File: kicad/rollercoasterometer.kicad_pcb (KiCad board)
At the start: 2 copper layers, 61 x 94 mm, 112 parts, among them J120 STANDOFF, J125 STANDOFF, J127 STANDOFF, J129 STANDOFF, J1401 USB_C_Receptacle, J1402 USB_C_Receptacle, J1601 USB_C_Receptacle, J1602 USB_C_Receptacle, J401 SMA, Q2001 NMOS, Q3101 NMOS, Q801 NMOS, U1001 ADP122 1.8V, U104 Teensy4.1, U1101 BMM150, U1201 ICM-42688, U1301 ICM-42688, U1801 TLE493D-W2B6, U1901 ADP122 1.8V, U201 ICM-42688, U2101 ICM-42688, U2201 BMM150, U2401 AK09918, U2501 BMP384, U2701 ICM-42688, U2801 TLE493D-W2B6, U2901 BMP384, U3001 ADP122 1.8V, U301 USBLC6-2SC6, U3201 ICM-42688, U3301 BMM150, U3401 AK09918, U401 ZED_F9R, U501 ADP122 1.8V, U601 AK09918, U704 TLE493D-W2B6, U901 BMP384

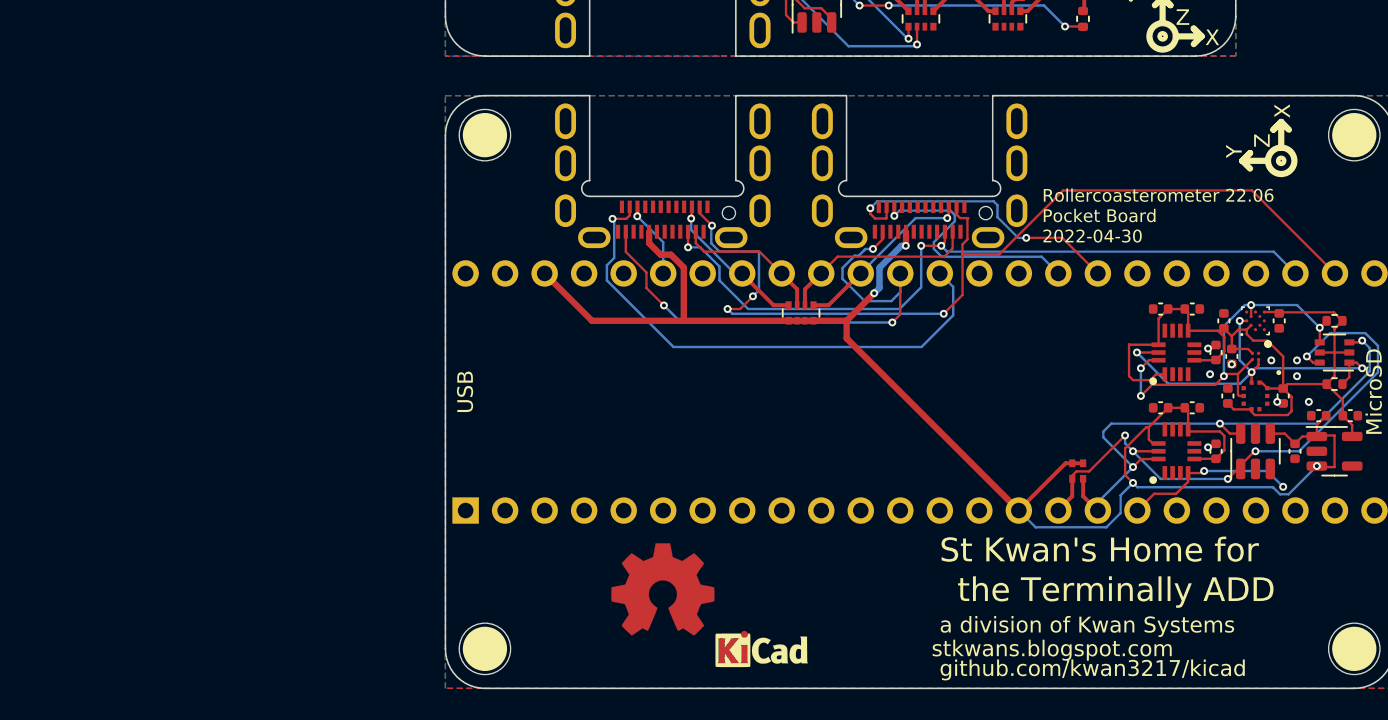
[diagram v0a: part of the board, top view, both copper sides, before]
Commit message: Broke down sensor block into a tree of sheets
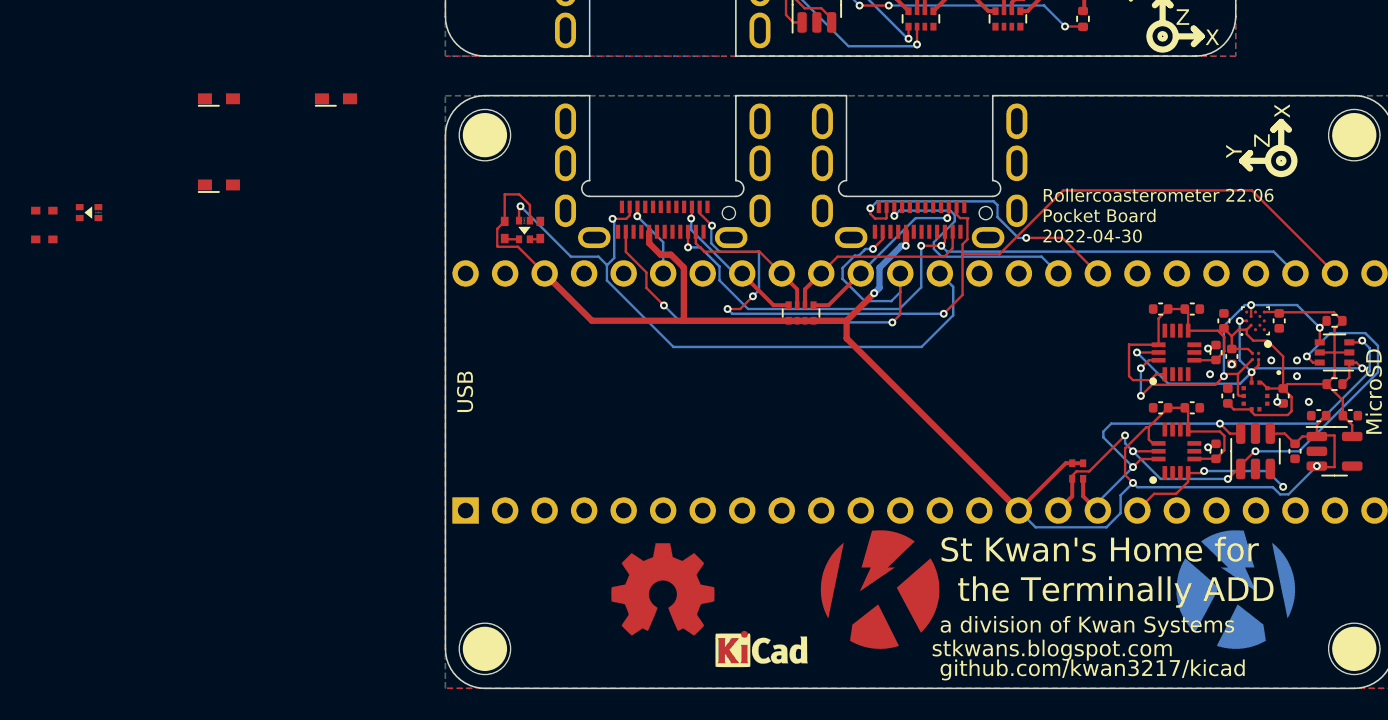
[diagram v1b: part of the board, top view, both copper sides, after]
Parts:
- added D1001: RED, KwanSystems:D_KINGBRIGHT, F.Cu at (69.2, 117.0)
- added D1401: GREEN, YELLOW, KwanSystems:LEDKingbrightAPHB, F.Cu at (81.3, 125.5)
- added D1601: GREEN, YELLOW, KwanSystems:LEDKingbrightAPHB, F.Cu at (53.3, 124.4)
- added D1905: RED, KwanSystems:D_KINGBRIGHT, F.Cu at (61.6, 122.6)
- added D3001: RED, KwanSystems:D_KINGBRIGHT, F.Cu at (61.6, 117.0)
- added R1401: 330, KwanSystems:SMD_0402, F.Cu at (82.3, 125.5)
- added R1402: 1k, KwanSystems:SMD_0402, F.Cu at (80.0, 125.5)
- added R1601: 330, KwanSystems:SMD_0402, F.Cu at (50.4, 124.2)
- added R1602: 1k, KwanSystems:SMD_0402, F.Cu at (50.4, 126.1)
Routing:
- net +3V3: track 105.2 -> 115.4 mm
- net /P0_ID: track 33.9 -> 42.0 mm, vias 1 -> 2
- net /Shoe/USB+ cable/DY-: track 0.00 -> 0.94 mm
- net /Shoe/USB+ cable/DG-: track 0.00 -> 0.69 mm

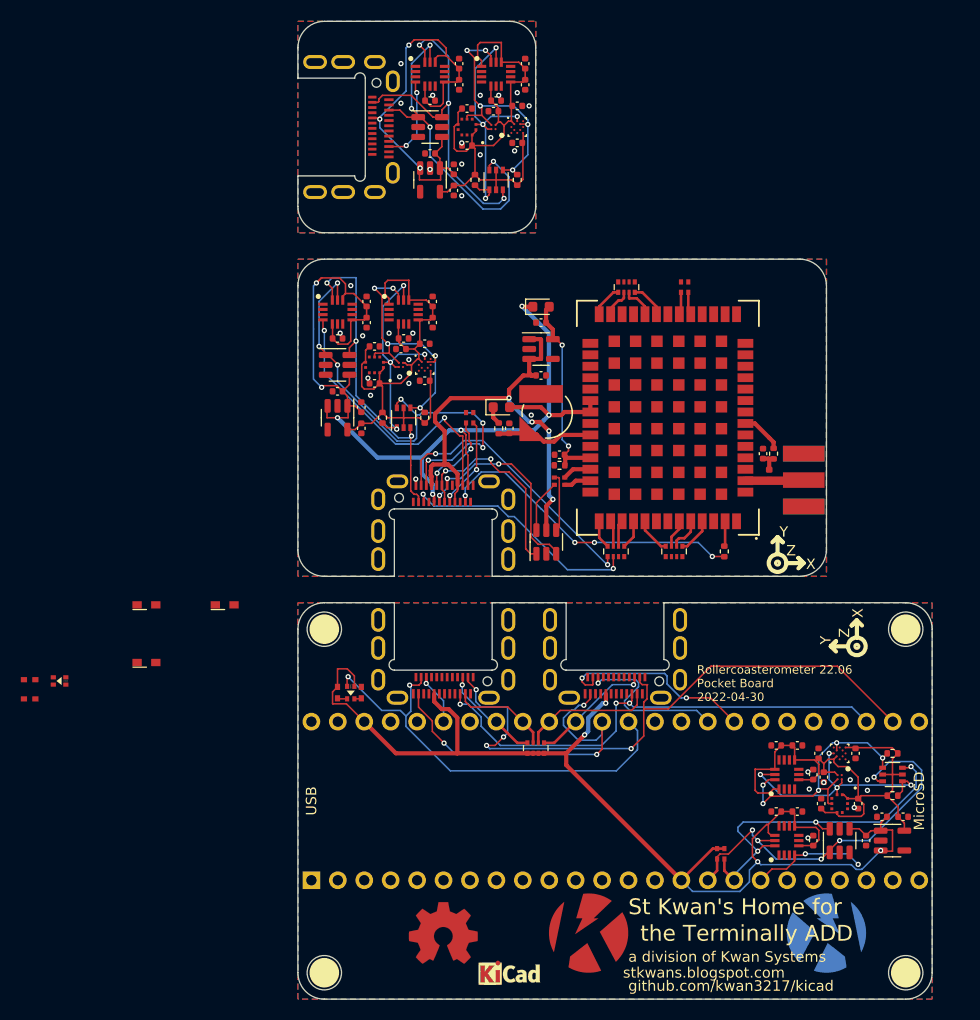
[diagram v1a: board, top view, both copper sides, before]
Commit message: One shining moment
Commit board while it still works
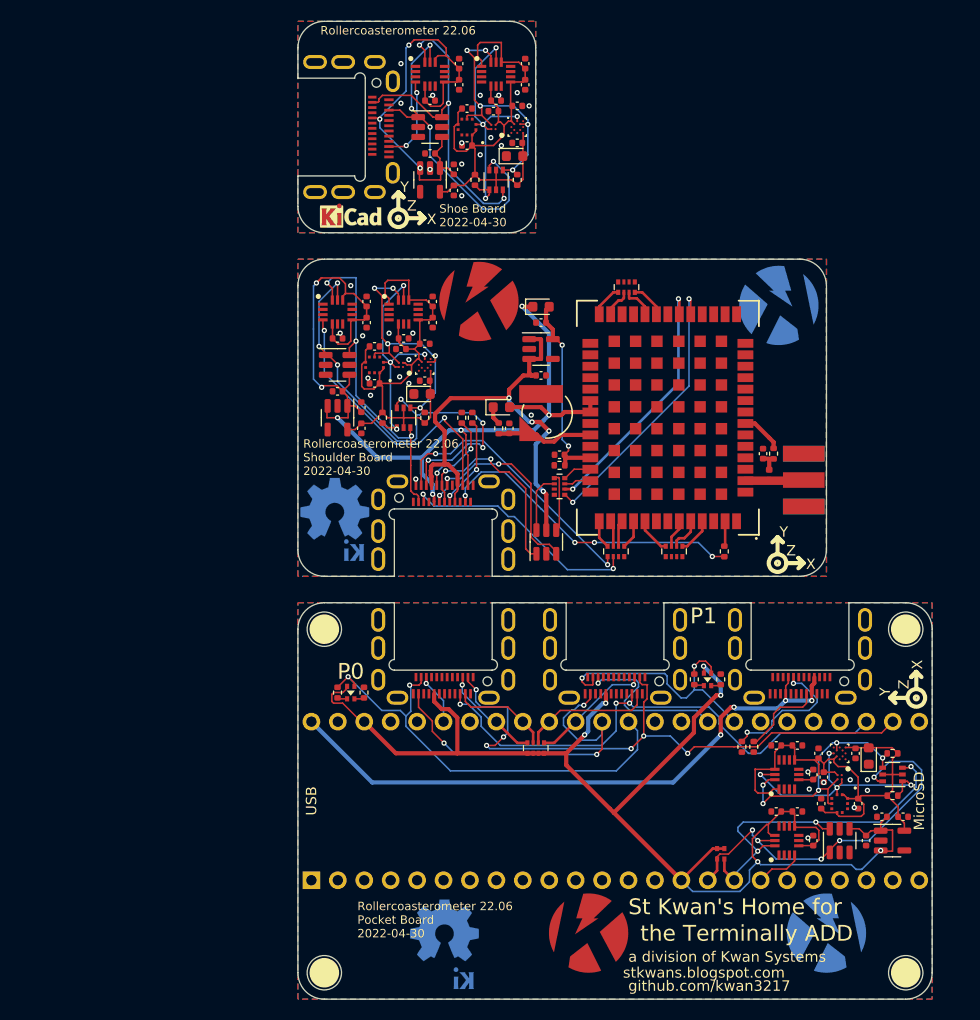
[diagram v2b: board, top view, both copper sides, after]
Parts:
- removed the R439 at (101.3, 105.2)
- added G1501: DesignedWithKicad, KwanSystems:Symbol_KiCAD-Logo_CopperAndSilkScreenTop_small, F.Cu at (81.3, 79.6)
- added G1505: Axis, KwanSystems:Axis, F.Cu at (85.9, 79.9)
- added G301: KwanSystems, KwanSystems:StKwansSoldermask, F.Cu at (93.6, 87.9)
- added G302: KwanSystems, KwanSystems:StKwansSoldermask, B.Cu at (122.4, 88.3)
- added G303: DesignedWithKicad, KwanSystems:Symbol_KiCAD-Logo_CopperAndSilkScreenTop_small, B.Cu at (79.8, 111.9)
- added G304: OSHW, KwanSystems:OSHW-Symbol_6.7x6mm_SolderMask, B.Cu at (79.8, 107.8)
- added J101: USB_C_Receptacle, KwanSystems:USB_C_Amphenol_MidMount, F.Cu at (124.5, 116.8)
- added R101: 5.1k, Resistor_SMD:R_0402_1005Metric, F.Cu at (120.0, 130.7)
- added R102: 5.1k, Resistor_SMD:R_0402_1005Metric, F.Cu at (118.9, 130.7)
- added R302: 5.1k, Resistor_SMD:R_0402_1005Metric, F.Cu at (93.0, 99.1)
- D1001, D1905, D3001: footprint KwanSystems:D_KINGBRIGHT -> LED_SMD:LED_0603_1608Metric
- G103, G104: moved to B.Cu
- R1401, R1402, R1601, R1602: footprint KwanSystems:SMD_0402 -> Resistor_SMD:R_0402_1005Metric
- R301: footprint KwanSystems:R_Array_Convex_2x0402 -> Resistor_SMD:R_0402_1005Metric
- R439: renamed from R411; footprint KwanSystems:R_Array_Convex_2x0402 -> KwanSystems:R_Array_Convex_4x0402
- U1101, U2201, U3301: footprint Package_CSP:WLCSP-12_1.56x1.56mm_P0.4mm -> KwanSystems:BMM150
- U501: value ADP122 1.8V -> ADP122 3.3V
- moved D3001 70.9 mm to (131.1, 131.6), turned to 90 degrees
- moved R1601 66.4 mm to (116.8, 124.2), turned to 90 degrees
- moved R1602 63.9 mm to (114.3, 124.2), turned to 90 degrees
- moved D1601 62.3 mm to (115.6, 124.2), turned to 90 degrees
- moved D1905 60.2 mm to (97.0, 73.9)
- moved D1001 27.8 mm to (88.1, 96.8)
- moved R439 22.6 mm to (101.3, 105.7), turned to 0 degrees
- moved G105 7.56 mm to (135.6, 126.0)
- moved G103 6.26 mm to (90.3, 153.0), turned to 180 degrees
- moved R301 0.76 mm to (91.9, 99.1)
- moved G104 0.28 mm to (90.3, 148.3), turned to 180 degrees
- moved R1401 0.25 mm to (82.5, 125.5)
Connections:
- D1401 pad 1: +3V3 -> /P0_ID
- D1401 pad 3: /P0_ID -> +3V3
- D1601 pad 1: +3V3 -> /P1_ID
- D1601 pad 3: /P1_ID -> +3V3
- R1402 pad 2: +3V3 -> /P0_ID
- R1602 pad 2: +3V3 -> /P1_ID
- R301 pad 2: /Shoulder/Q_CC2 -> /Shoulder/Q_GND
- R439 pad 1: /Shoulder/GPS Rover/RTK_STAT- -> /Shoulder/R_D-
- R439 pad 2: /Shoulder/GPS Rover/GEOFENCE_STAT- -> /Shoulder/R_D+
- R439 pad 3: /Shoulder/GPS Rover/GEOFENCE -> /Shoulder/GPS Rover/RTK
- R439 pad 4: /Shoulder/GPS Rover/RTK -> /Shoulder/GPS Rover/GEOFENCE
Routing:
- net +5V: track 0.00 -> 59.6 mm, vias 0 -> 4
- net /Shoulder/GPS Rover/GEOFENCE_STAT-: track 2.20 -> 27.1 mm, vias 0 -> 2
- net /Shoulder/GPS Rover/RTK_STAT-: track 2.17 -> 25.0 mm, vias 0 -> 2
- net +3V3: track 115.4 -> 131.7 mm, vias 4 -> 6
- net /CC2: track 0.00 -> 13.3 mm, vias 0 -> 2
- net /CC1: track 0.00 -> 8.11 mm
- net /P2_INT: track 11.3 -> 4.59 mm, vias 2 -> 0
- net /P1_ID: track 19.4 -> 25.8 mm
- net /RX_GPS: track 47.2 -> 50.1 mm
- net /TX_GPS: track 61.0 -> 59.0 mm, vias 4 -> 6
- net /Shoulder/GPS Rover/RF_IN: track 6.89 -> 5.21 mm
- net /P0_ID: track 42.0 -> 43.6 mm
- net /Shoulder/USB+ cable/DY-: track 0.00 -> 0.87 mm
- net /Shoulder/USB+ cable/DG-: track 0.00 -> 0.87 mm
- net /Shoulder/R_D+: track 5.07 -> 5.76 mm
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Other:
- outline, holes or cut-outs redrawn
- board text added: "P0"
- board text added: "P1"
- board text added: "Rollercoasterometer 22.06"
- board text added: "Rollercoasterometer 22.06 Shoulder Board 2022-04-30"
- board text added: "Shoe Board 2022-04-30"
- board text added: "St Kwan's Home for the Terminally ADD"
- board text added: "a division of Kwan Systems stkwans.blogspot.com github.com/kwan3217"

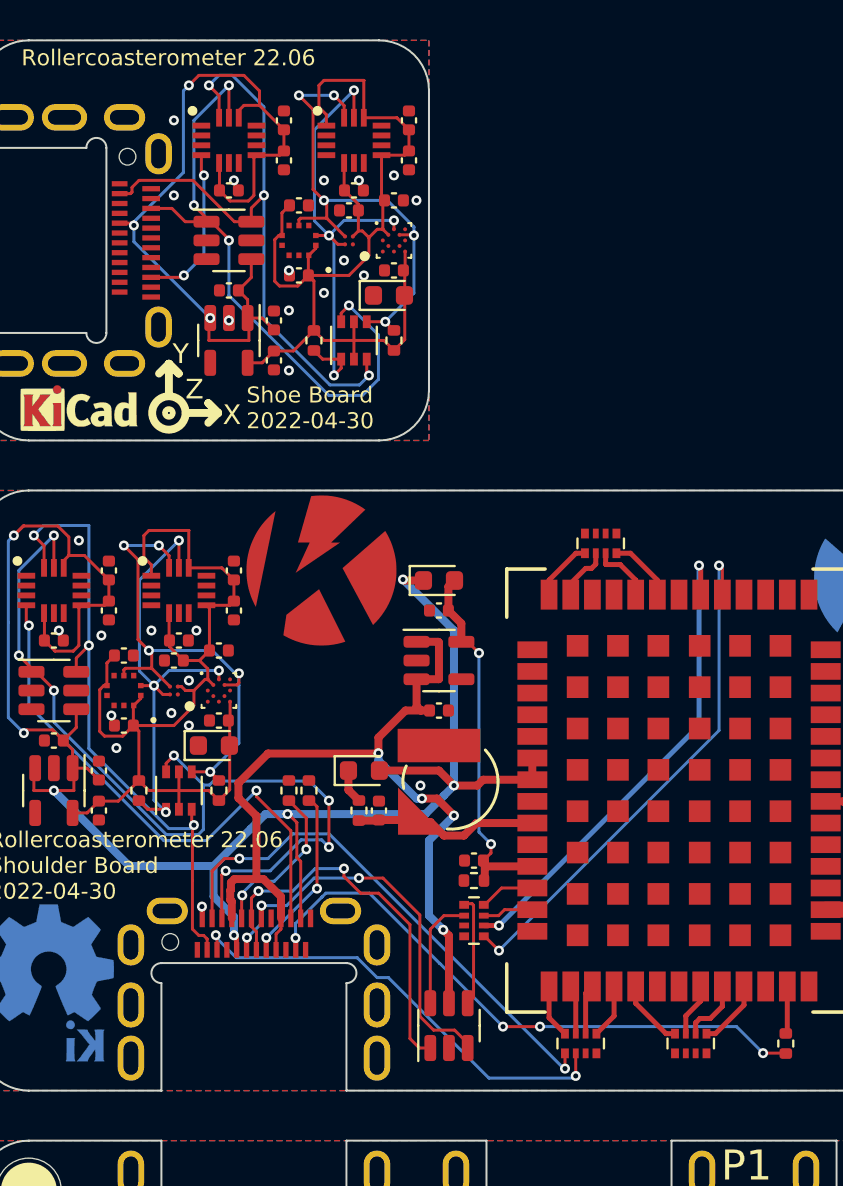
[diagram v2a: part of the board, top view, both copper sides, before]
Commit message: Updating PCB to follow schematic
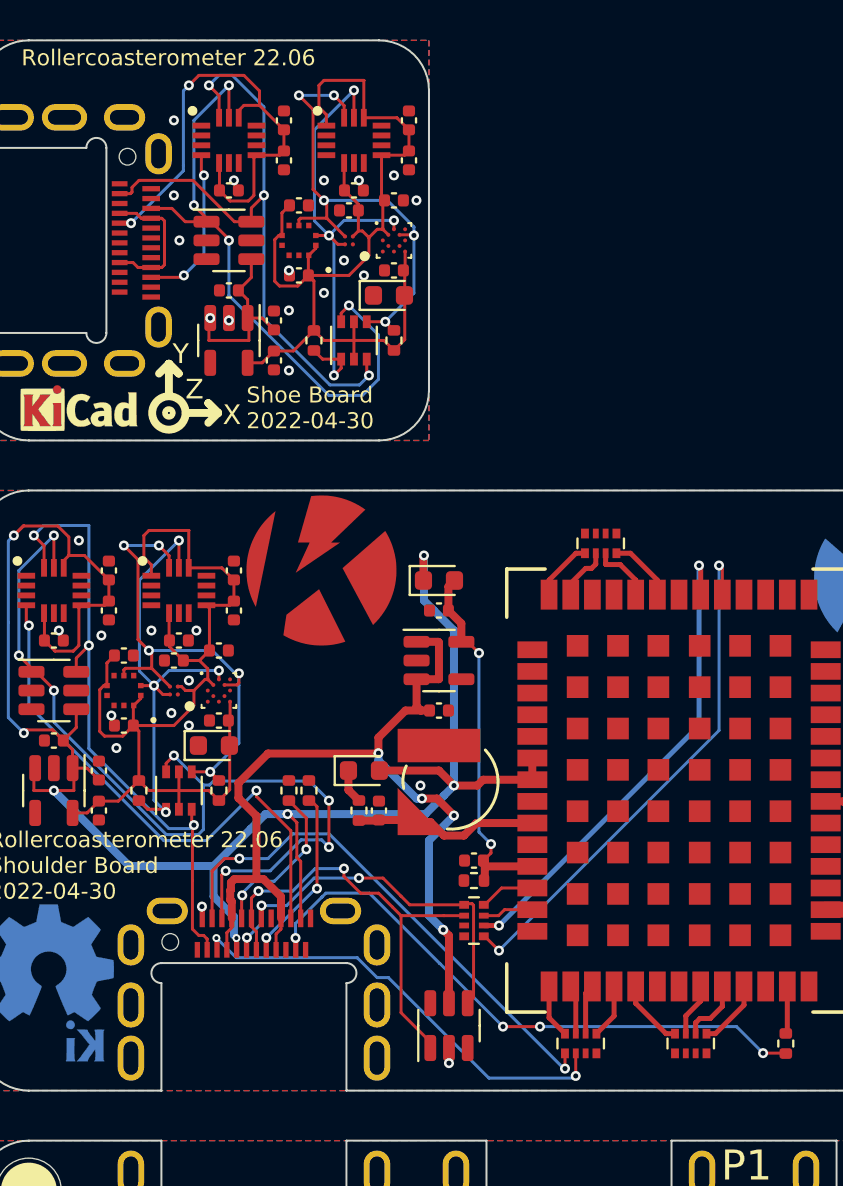
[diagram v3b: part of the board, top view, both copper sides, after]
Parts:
- R2001, R2002, R3101, R3102, R801, R802: value 2.2k -> 5.1k
- R436: value 3.3k -> 5.1k
- U1001, U1901, U3001: value ADP122 1.8V -> TCR2EF 1.8V
- U301: value USBLC6-2SC6 -> NSP4201MR6
- U501: value ADP122 3.3V -> TCR2EF 3.3V
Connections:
- J1401 pad A9: unconnected-(J1401-PadA4) -> (no net)
- J1401 pad B4: unconnected-(J1401-PadA4) -> (no net)
- J1401 pad B9: unconnected-(J1401-PadA4) -> (no net)
- J1601 pad A9: unconnected-(J1601-PadA4) -> (no net)
- J1601 pad B4: unconnected-(J1601-PadA4) -> (no net)
- J1601 pad B9: unconnected-(J1601-PadA4) -> (no net)
- R439 pad 1: /Shoulder/R_D- -> /Shoulder/Q_D-
- R439 pad 2: /Shoulder/R_D+ -> /Shoulder/Q_D+
- U301 pad 3: /Shoulder/Q_D- -> unconnected-(U301-Pad3)
- U301 pad 4: /Shoulder/R_D- -> /Shoulder/Q_D-
- U301 pad 6: /Shoulder/R_D+ -> unconnected-(U301-Pad6)
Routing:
- net /Shoe/USB+ cable/Q_VBUS: track 0.00 -> 7.10 mm
- net /Shoe/Q_3V3: track 41.0 -> 34.5 mm
- net /Shoulder/R_D+: track 5.76 -> 0.00 mm
- net /Shoulder/R_D-: track 5.61 -> 0.00 mm
- net /Shoulder/Q_D+: track 19.8 -> 22.7 mm
- net /Shoulder/Q_VBUS: track 46.3 -> 48.0 mm
- net /Shoulder/Q_3V3: track 94.3 -> 95.1 mm
- net /Shoulder/Q_GND: track 0.00 -> 0.77 mm, vias 12 -> 13
- net /Shoe/Q_GND: vias 14 -> 15
